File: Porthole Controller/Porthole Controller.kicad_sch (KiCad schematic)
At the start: 19 parts, among them J1 Conn_02x03_Counter_Clockwise, J2 Conn_01x03, J3 Screw_Terminal_01x03, J4 Screw_Terminal_01x03, J5 Screw_Terminal_01x03, J6 Screw_Terminal_01x03, J7 Screw_Terminal_01x02, SW1 SW_Push, U1 113991054, U2 SN74AHCT125DR

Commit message: Completed schematic
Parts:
- removed J2: Conn_01x03, symbol Connector_Generic:Conn_01x03
- removed SW1: SW_Push, symbol Switch:SW_Push
- added J2: Conn_02x04_Top_Bottom, symbol Connector_Generic:Conn_02x04_Top_Bottom
- added J8: Conn_01x04, symbol Connector_Generic:Conn_01x04
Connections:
- net L/R is gone; now on net GND: J1.1 (Pin_1)
- net 3.3V: now also J2.1 (Pin_1), J2.2 (Pin_2), J2.3 (Pin_3), J2.4 (Pin_4)
- net GND: now also J2.5 (Pin_5), J2.6 (Pin_6), J2.7 (Pin_7), J2.8 (Pin_8)
- net SCK: now also U1.10 (D9)
- net SD: now also U1.11 (D10)
- net WS: now also U1.9 (D8)
- net D0: now reaches U1.1 (D0)
- net D0: now also J8.1 (Pin_1)
- net D1: now reaches U1.2 (D1)
- net D1: now also J8.2 (Pin_2)
- net D2: now reaches U1.3 (D2)
- net D2: now also U2.2 (1A)
- net D3: now reaches U1.4 (D3)
- net D3: now also U2.5 (2A)
- net D4: now reaches U1.5 (D4)
- net D4: now also J8.3 (Pin_3)
- net D5: now reaches U1.6 (D5)
- net D5: now also J8.4 (Pin_4)
- net D6: now reaches U1.7 (TX_D6)
- net D6: now also U2.9 (3A)
- net D7: now reaches U1.8 (RX_D7)
- net D7: now also U2.12 (4A)
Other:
- moved on the sheet: J1, U1

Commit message: Prototype board designed
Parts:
- C1: value C -> 100nF; footprint (none) -> Capacitor_THT:C_Disc_D3.0mm_W1.6mm_P2.50mm
- C2, C3, C4, C5: value C_Polarized -> 1000uF; footprint (none) -> Capacitor_THT:CP_Radial_D6.3mm_P2.50mm
- J1: renamed from J3; value Screw_Terminal_01x03 -> STRIP1; footprint (none) -> TerminalBlock:TerminalBlock_bornier-3_P5.08mm
- J2: renamed from J4; value Screw_Terminal_01x03 -> STRIP2; footprint (none) -> TerminalBlock:TerminalBlock_bornier-3_P5.08mm
- J3: renamed from J5; value Screw_Terminal_01x03 -> STRIP3; footprint (none) -> TerminalBlock:TerminalBlock_bornier-3_P5.08mm
- J4: renamed from J6; value Screw_Terminal_01x03 -> STRIP4; footprint (none) -> TerminalBlock:TerminalBlock_bornier-3_P5.08mm
- J5: renamed from J1; value Conn_02x03_Counter_Clockwise -> INMP441; footprint (none) -> Connector_PinSocket_2.54mm:PinSocket_2x03_P2.54mm_Vertical; symbol Connector_Generic:Conn_02x03_Counter_Clockwise -> Connector_Generic:Conn_02x03_Odd_Even
- J6: renamed from J2; footprint (none) -> Connector_PinSocket_2.54mm:PinSocket_2x04_P2.54mm_Vertical; symbol Connector_Generic:Conn_02x04_Top_Bottom -> Connector_Generic:Conn_02x04_Odd_Even
- J7: value Screw_Terminal_01x02 -> - +; footprint (none) -> TerminalBlock:TerminalBlock_bornier-2_P5.08mm
- J8: footprint (none) -> Connector_PinSocket_2.54mm:PinSocket_1x04_P2.54mm_Vertical
- R1, R2, R3, R4: value R -> 100; footprint (none) -> Resistor_THT:R_Axial_DIN0204_L3.6mm_D1.6mm_P5.08mm_Horizontal
- U1: footprint 113991054:MODULE_113991054 -> symbols:xiaoesp32_c3_MM
- U2: footprint SN74AHCT125DR:SOIC127P600X175-14N -> symbols:N14_TEX
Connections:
- net 3.3V: now also J5.4 (Pin_4), J6.5 (Pin_5), J6.7 (Pin_7); no longer J5.5 (Pin_5), J6.2 (Pin_2), J6.4 (Pin_4)
- net GND: now also J5.2 (Pin_2), J6.2 (Pin_2), J6.4 (Pin_4); no longer J5.6 (Pin_6), J6.5 (Pin_5), J6.7 (Pin_7)
- net SCK: now also J5.5 (Pin_5); no longer J5.3 (Pin_3)
- net SD: now also J5.6 (Pin_6); no longer J5.4 (Pin_4)
- net WS: now also J5.3 (Pin_3); no longer J5.2 (Pin_2)
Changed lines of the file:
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@@
 	)
 	(symbol
-		(lib_id "Connector_Generic:Conn_02x04_Top_Bottom")
+		(lib_id "Connector_Generic:Conn_02x04_Odd_Even")
 		(at 85.09 142.24 0)
 		(unit 1)
@@
 		(dnp no)
 		(fields_autoplaced yes)
-		(property "Reference" "J2"
+		(property "Reference" "J6"
 			(at 86.36 133.35 0)
 			(effects
@@
 			)
 		)
-		(property "Footprint" ""
+		(property "Footprint" "Connector_PinSocket_2.54mm:PinSocket_2x04_P2.54mm_Vertical"
 			(at 85.09 142.24 0)
 			(effects
@@
 			)
 		)
-		(property "Description" "Generic connector, double row, 02x04, top/bottom pin numbering scheme (row 1: 1...pins_per_row, row2: pins_per_row+1 ... num_pins), script generated (kicad-library-utils/schlib/autogen/connector/)"
+		(property "Description" "Generic connector, double row, 02x04, odd/even pin numbering scheme (row 1 odd numbers, row 2 even numbers), script generated (kicad-library-utils/schlib/autogen/connector/)"
 			(at 85.09 142.24 0)
 			(effects
@@
 			(project "Porthole Controller"
 				(path "/13f1af3d-398f-4c37-b3cd-b8dafcc64830"
-					(reference "J2")
+					(reference "J6")
 					(unit 1)
 				)
@@
 			)
 		)
-		(property "Footprint" ""
+		(property "Footprint" "Connector_PinSocket_2.54mm:PinSocket_1x04_P2.54mm_Vertical"
 			(at 58.42 142.24 0)
 			(effects
@@
 			)
 		)
-		(property "Value" "C_Polarized"
+		(property "Value" "1000uF"
 			(at 207.01 141.3509 0)
 			(effects
@@
 			)
 		)
-		(property "Footprint" ""
+		(property "Footprint" "Capacitor_THT:CP_Radial_D6.3mm_P2.50mm"
 			(at 204.1652 144.78 0)
 			(effects
@@
 		(on_board yes)
 		(dnp no)
-		(fields_autoplaced yes)
 		(property "Reference" "R1"
-			(at 220.9801 40.64 0)
-			(effects
-				(font
-					(size 1.27 1.27)
-				)
-				(justify left)
-			)
-		)
-		(property "Value" "R"
-			(at 218.4401 40.64 0)
-			(effects
-				(font
-					(size 1.27 1.27)
-				)
-				(justify left)
-			)
-		)
-		(property "Footprint" ""
+			(at 219.964 35.814 90)
+			(effects
+				(font
+					(size 1.27 1.27)
+				)
+			)
+		)
+		(property "Value" "100"
+			(at 219.71 38.1 90)
+			(effects
+				(font
+					(size 1.27 1.27)
+				)
+			)
+		)
+		(property "Footprint" "Resistor_THT:R_Axial_DIN0204_L3.6mm_D1.6mm_P5.08mm_Horizontal"
 			(at 219.71 36.322 90)
 			(effects
@@
 			)
 		)
-		(property "Value" "C_Polarized"
+		(property "Value" "1000uF"
 			(at 207.01 115.9509 0)
 			(effects
@@
 			)
 		)
-		(property "Footprint" ""
+		(property "Footprint" "Capacitor_THT:CP_Radial_D6.3mm_P2.50mm"
 			(at 204.1652 119.38 0)
 			(effects
@@
 			)
 		)
-		(property "Value" "C"
+		(property "Value" "100nF"
 			(at 210.82 55.8799 0)
 			(effects
@@
 			)
 		)
-		(property "Footprint" ""
+		(property "Footprint" "Capacitor_THT:C_Disc_D3.0mm_W1.6mm_P2.50mm"
 			(at 207.9752 58.42 0)
 			(effects
@@
 			)
 		)
-		(property "Value" "Screw_Terminal_01x02"
+		(property "Value" "-   +"
 			(at 110.49 36.8299 0)
 			(effects
@@
 			)
 		)
-		(property "Footprint" ""
+		(property "Footprint" "TerminalBlock:TerminalBlock_bornier-2_P5.08mm"
 			(at 107.95 34.29 0)
 			(effects
@@
 		(on_board yes)
 		(dnp no)
-		(fields_autoplaced yes)
 		(property "Reference" "R4"
-			(at 220.9801 63.5 0)
-			(effects
-				(font
-					(size 1.27 1.27)
-				)
-				(justify left)
-			)
-		)
-		(property "Value" "R"
-			(at 218.4401 63.5 0)
-			(effects
-				(font
-					(size 1.27 1.27)
-				)
-				(justify left)
-			)
-		)
-		(property "Footprint" ""
+			(at 219.71 58.674 90)
+			(effects
+				(font
+					(size 1.27 1.27)
+				)
+			)
+		)
+		(property "Value" "100"
+			(at 219.71 60.96 90)
+			(effects
+				(font
+					(size 1.27 1.27)
+				)
+			)
+		)
+		(property "Footprint" "Resistor_THT:R_Axial_DIN0204_L3.6mm_D1.6mm_P5.08mm_Horizontal"
 			(at 219.71 59.182 90)
 			(effects
@@
 	)
 	(symbol
-		(lib_id "Connector_Generic:Conn_02x03_Counter_Clockwise")
+		(lib_id "Connector_Generic:Conn_02x03_Odd_Even")
 		(at 135.89 96.52 0)
 		(unit 1)
@@
 		(dnp no)
 		(fields_autoplaced yes)
-		(property "Reference" "J1"
+		(property "Reference" "J5"
 			(at 137.16 87.63 0)
 			(effects
@@
 			)
 		)
-		(property "Value" "Conn_02x03_Counter_Clockwise"
+		(property "Value" "INMP441"
 			(at 137.16 90.17 0)
 			(effects
@@
 			)
 		)
-		(property "Footprint" ""
+		(property "Footprint" "Connector_PinSocket_2.54mm:PinSocket_2x03_P2.54mm_Vertical"
 			(at 135.89 96.52 0)
 			(effects
@@
 			)
 		)
-		(property "Description" "Generic connector, double row, 02x03, counter clockwise pin numbering scheme (similar to DIP package numbering), script generated (kicad-library-utils/schlib/autogen/connector/)"
+		(property "Description" "Generic connector, double row, 02x03, odd/even pin numbering scheme (row 1 odd numbers, row 2 even numbers), script generated (kicad-library-utils/schlib/autogen/connector/)"
 			(at 135.89 96.52 0)
 			(effects
@@
 			(project "Porthole Controller"
 				(path "/13f1af3d-398f-4c37-b3cd-b8dafcc64830"
-					(reference "J1")
+					(reference "J5")
 					(unit 1)
 				)
@@
 			)
 		)
-		(property "Value" "C_Polarized"
+		(property "Value" "1000uF"
 			(at 207.01 101.9809 0)
 			(effects
@@
 			)
 		)
-		(property "Footprint" ""
+		(property "Footprint" "Capacitor_THT:CP_Radial_D6.3mm_P2.50mm"
 			(at 204.1652 105.41 0)
 			(effects
@@
 		(dnp no)
 		(fields_autoplaced yes)
-		(property "Reference" "J3"
+		(property "Reference" "J1"
 			(at 223.52 100.3299 0)
 			(effects
@@
 			)
 		)
-		(property "Value" "Screw_Terminal_01x03"
+		(property "Value" "STRIP1"
 			(at 223.52 102.8699 0)
 			(effects
@@
 			)
 		)
-		(property "Footprint" ""
+		(property "Footprint" "TerminalBlock:TerminalBlock_bornier-3_P5.08mm"
 			(at 220.98 101.6 0)
 			(effects
@@
 			(project "Porthole Controller"
 				(path "/13f1af3d-398f-4c37-b3cd-b8dafcc64830"
-					(reference "J3")
+					(reference "J1")
 					(unit 1)
 				)
@@
 		(on_board yes)
 		(dnp no)
-		(fields_autoplaced yes)
 		(property "Reference" "R2"
-			(at 220.9801 48.26 0)
-			(effects
-				(font
-					(size 1.27 1.27)
-				)
-				(justify left)
-			)
-		)
-		(property "Value" "R"
-			(at 218.4401 48.26 0)
-			(effects
-				(font
-					(size 1.27 1.27)
-				)
-				(justify left)
-			)
-		)
-		(property "Footprint" ""
+			(at 218.186 43.434 90)
+			(effects
+				(font
+					(size 1.27 1.27)
+				)
+				(justify left)
+			)
+		)
+		(property "Value" "100"
+			(at 217.678 45.72 90)
+			(effects
+				(font
+					(size 1.27 1.27)
+				)
+				(justify left)
+			)
+		)
+		(property "Footprint" "Resistor_THT:R_Axial_DIN0204_L3.6mm_D1.6mm_P5.08mm_Horizontal"
 			(at 219.71 43.942 90)
 			(effects
@@
 		(dnp no)
 		(fields_autoplaced yes)
-		(property "Reference" "J5"
+		(property "Reference" "J3"
 			(at 223.52 125.7299 0)
 			(effects
@@
 			)
 		)
-		(property "Value" "Screw_Terminal_01x03"
+		(property "Value" "STRIP3"
 			(at 223.52 128.2699 0)
 			(effects
@@
 			)
 		)
-		(property "Footprint" ""
+		(property "Footprint" "TerminalBlock:TerminalBlock_bornier-3_P5.08mm"
 			(at 220.98 127 0)
 			(effects
@@
 			(project "Porthole Controller"
 				(path "/13f1af3d-398f-4c37-b3cd-b8dafcc64830"
-					(reference "J5")
+					(reference "J3")
 					(unit 1)
 				)
@@
 			)
 		)
-		(property "Value" "C_Polarized"
+		(property "Value" "1000uF"
 			(at 207.01 127.3809 0)
 			(effects
@@
 			)
 		)
-		(property "Footprint" ""
+		(property "Footprint" "Capacitor_THT:CP_Radial_D6.3mm_P2.50mm"
 			(at 204.1652 130.81 0)
 			(effects
@@
 		(on_board yes)
 		(dnp no)
-		(fields_autoplaced yes)
 		(property "Reference" "R3"
-			(at 220.9801 55.88 0)
-			(effects
-				(font
-					(size 1.27 1.27)
-				)
-				(justify left)
-			)
-		)
-		(property "Value" "R"
-			(at 218.4401 55.88 0)
-			(effects
-				(font
-					(size 1.27 1.27)
-				)
-				(justify left)
-			)
-		)
-		(property "Footprint" ""
+			(at 219.964 51.054 90)
+			(effects
+				(font
+					(size 1.27 1.27)
+				)
+			)
+		)
+		(property "Value" "100"
+			(at 219.71 53.34 90)
+			(effects
+				(font
+					(size 1.27 1.27)
+				)
+			)
+		)
+		(property "Footprint" "Resistor_THT:R_Axial_DIN0204_L3.6mm_D1.6mm_P5.08mm_Horizontal"
 			(at 219.71 51.562 90)
 			(effects
@@
 			)
 		)
-		(property "Footprint" "113991054:MODULE_113991054"
+		(property "Footprint" "symbols:xiaoesp32_c3_MM"
 			(at 83.82 99.06 0)
 			(effects
@@
 			)
 		)
-		(property "Footprint" "SN74AHCT125DR:SOIC127P600X175-14N"
+		(property "Footprint" "symbols:N14_TEX"
 			(at 184.15 48.26 0)
 			(effects
@@
 		(dnp no)
 		(fields_autoplaced yes)
-		(property "Reference" "J4"
+		(property "Reference" "J2"
 			(at 223.52 114.2999 0)
 			(effects
@@
 			)
 		)
-		(property "Value" "Screw_Terminal_01x03"
+		(property "Value" "STRIP2"
 			(at 223.52 116.8399 0)
 			(effects
@@
 			)
 		)
-		(property "Footprint" ""
+		(property "Footprint" "TerminalBlock:TerminalBlock_bornier-3_P5.08mm"
 			(at 220.98 115.57 0)
 			(effects
@@
 			(project "Porthole Controller"
 				(path "/13f1af3d-398f-4c37-b3cd-b8dafcc64830"
-					(reference "J4")
+					(reference "J2")
 					(unit 1)
 				)
@@
 		(dnp no)
 		(fields_autoplaced yes)
-		(property "Reference" "J6"
+		(property "Reference" "J4"
 			(at 223.52 139.6999 0)
 			(effects
@@
 			)
 		)
-		(property "Value" "Screw_Terminal_01x03"
+		(property "Value" "STRIP4"
 			(at 223.52 142.2399 0)
 			(effects
@@
 			)
 		)
-		(property "Footprint" ""
+		(property "Footprint" "TerminalBlock:TerminalBlock_bornier-3_P5.08mm"
 			(at 220.98 140.97 0)
 			(effects
@@
 			(project "Porthole Controller"
 				(path "/13f1af3d-398f-4c37-b3cd-b8dafcc64830"
-					(reference "J6")
-					(unit 1)
-				)
+					(reference "J4")
+					(unit 1)
+				)

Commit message: Updated footprints
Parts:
- C2, C3, C4, C5: footprint Capacitor_THT:CP_Radial_D6.3mm_P2.50mm -> Capacitor_THT:CP_Radial_D8.0mm_P3.80mm
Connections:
- net 3.3V: now also J5.3 (Pin_3); no longer J5.4 (Pin_4)
- net SCK: now also J5.6 (Pin_6), U1.9 (D8); no longer J5.5 (Pin_5), U1.10 (D9)
- net SD: now also J5.5 (Pin_5); no longer J5.6 (Pin_6)
- net WS: now also J5.4 (Pin_4), U1.10 (D9); no longer J5.3 (Pin_3), U1.9 (D8)

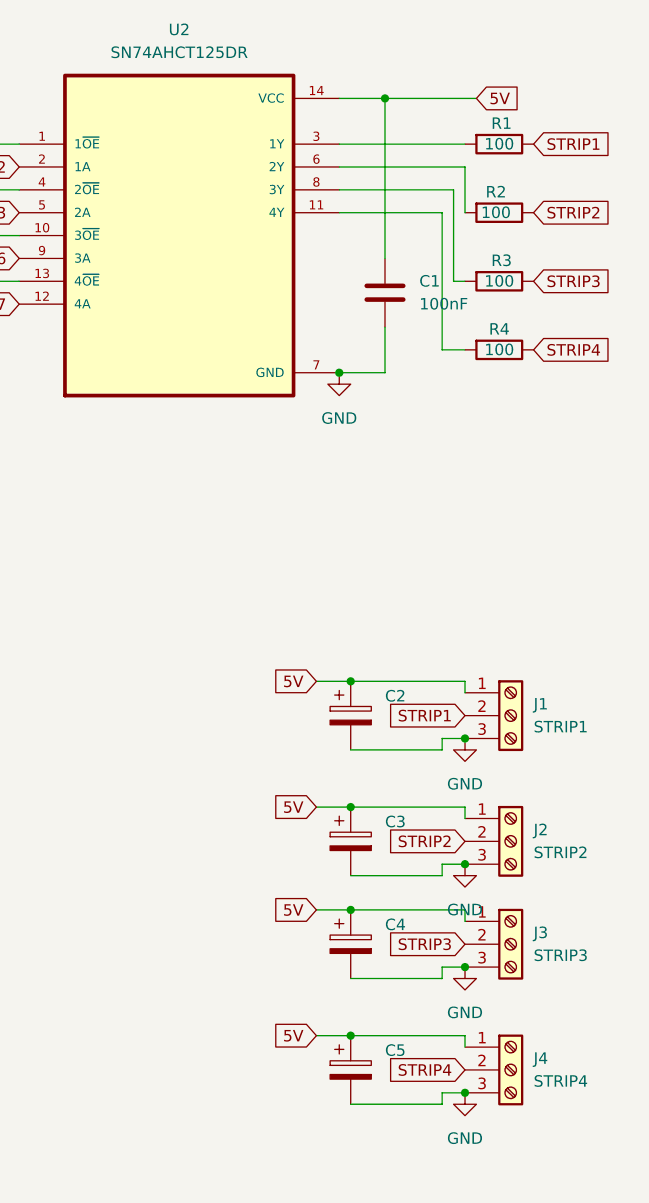
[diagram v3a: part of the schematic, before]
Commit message: bolden text, fix capacitor labels, reviewed DRC warnings
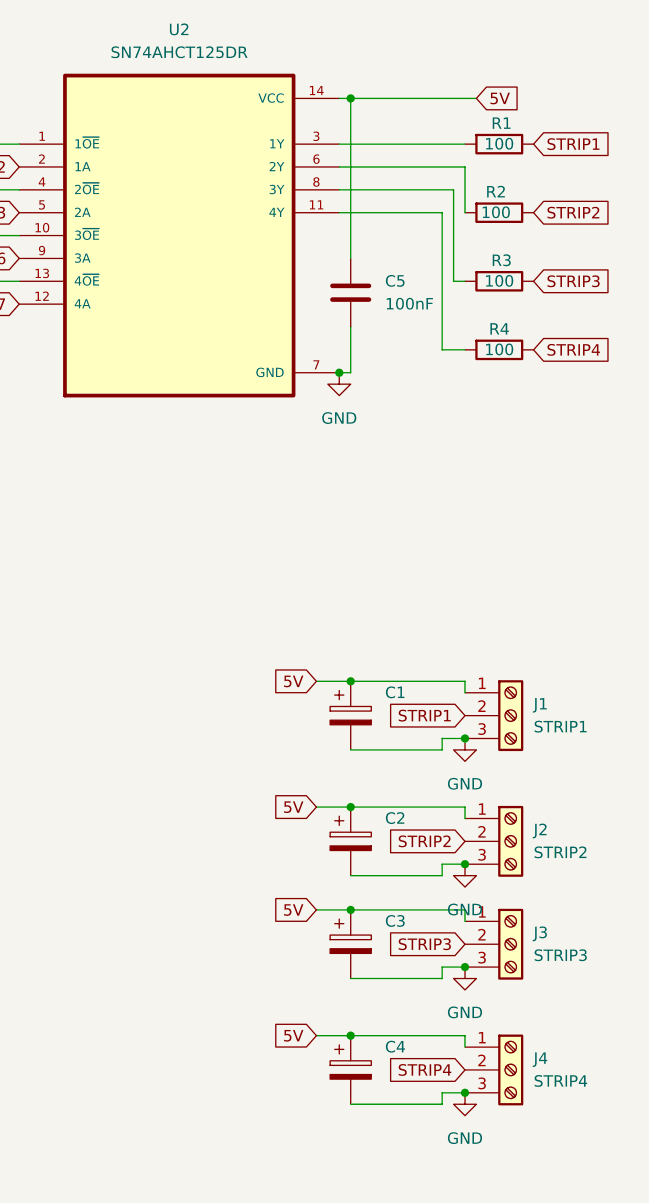
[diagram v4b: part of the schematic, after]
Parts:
- renumbered C2 to C1, C3 to C2, C4 to C3, C5 to C4, C1 to C5
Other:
- moved on the sheet: C5
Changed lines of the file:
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@@
 	)
 	(junction
-		(at 201.93 63.5)
+		(at 203.2 33.02)
 		(diameter 0)
 		(color 0 0 0 0)
 	)
 	(junction
-		(at 215.9 143.51)
+		(at 201.93 63.5)
 		(diameter 0)
 		(color 0 0 0 0)
 	)
 	(junction
-		(at 215.9 129.54)
+		(at 215.9 143.51)
 		(diameter 0)
 		(color 0 0 0 0)
 	)
 	(junction
-		(at 207.01 33.02)
+		(at 215.9 129.54)
 		(diameter 0)
 		(color 0 0 0 0)
@@
 	(wire
 		(pts
+			(xy 203.2 33.02) (xy 201.93 33.02)
+		)
+		(stroke
+			(width 0)
+			(type default)
+		)
+	)
+	(wire
+		(pts
 			(xy 215.9 111.76) (xy 215.9 113.03)
 		)
@@
 	(wire
 		(pts
-			(xy 207.01 63.5) (xy 201.93 63.5)
+			(xy 203.2 63.5) (xy 201.93 63.5)
 		)
 		(stroke
@@
 	(wire
 		(pts
-			(xy 207.01 58.42) (xy 207.01 63.5)
+			(xy 203.2 58.42) (xy 203.2 63.5)
 		)
 		(stroke
@@
 	(wire
 		(pts
-			(xy 207.01 50.8) (xy 207.01 33.02)
+			(xy 203.2 50.8) (xy 203.2 33.02)
 		)
 		(stroke
@@
 	(wire
 		(pts
-			(xy 203.2 123.19) (xy 215.9 123.19)
-		)
-		(stroke
-			(width 0)
-			(type default)
-		)
-	)
-	(wire
-		(pts
-			(xy 207.01 33.02) (xy 201.93 33.02)
+			(xy 203.2 33.02) (xy 217.17 33.02)
 		)
 		(stroke
@@
 	(wire
 		(pts
-			(xy 217.17 33.02) (xy 207.01 33.02)
+			(xy 203.2 123.19) (xy 215.9 123.19)
 		)
 		(stroke
@@
 		(on_board yes)
 		(dnp no)
-		(fields_autoplaced yes)
-		(property "Reference" "C5"
-			(at 207.01 138.8109 0)
+		(property "Reference" "C4"
+			(at 207.01 138.43 0)
 			(effects
 				(font
@@
 			(project "Porthole Controller"
 				(path "/13f1af3d-398f-4c37-b3cd-b8dafcc64830"
-					(reference "C5")
+					(reference "C4")
 					(unit 1)
 				)
@@
 		(on_board yes)
 		(dnp no)
-		(fields_autoplaced yes)
-		(property "Reference" "C3"
-			(at 207.01 113.4109 0)
+		(property "Reference" "C2"
+			(at 207.01 113.03 0)
 			(effects
 				(font
@@
 			(project "Porthole Controller"
 				(path "/13f1af3d-398f-4c37-b3cd-b8dafcc64830"
-					(reference "C3")
+					(reference "C2")
 					(unit 1)
 				)
@@
 	(symbol
 		(lib_id "Device:C")
-		(at 207.01 54.61 0)
+		(at 203.2 54.61 0)
 		(unit 1)
 		(exclude_from_sim no)
@@
 		(dnp no)
 		(fields_autoplaced yes)
-		(property "Reference" "C1"
-			(at 210.82 53.3399 0)
+		(property "Reference" "C5"
+			(at 207.01 53.3399 0)
 			(effects
 				(font
@@
 		)
 		(property "Value" "100nF"
-			(at 210.82 55.8799 0)
+			(at 207.01 55.8799 0)
 			(effects
 				(font
@@
 		)
 		(property "Footprint" "Capacitor_THT:C_Disc_D3.0mm_W1.6mm_P2.50mm"
-			(at 207.9752 58.42 0)
+			(at 204.1652 58.42 0)
 			(effects
 				(font
@@
 		)
 		(property "Datasheet" "~"
-			(at 207.01 54.61 0)
+			(at 203.2 54.61 0)
 			(effects
 				(font
@@
 		)
 		(property "Description" "Unpolarized capacitor"
-			(at 207.01 54.61 0)
+			(at 203.2 54.61 0)
 			(effects
 				(font
@@
 			(project "Porthole Controller"
 				(path "/13f1af3d-398f-4c37-b3cd-b8dafcc64830"
-					(reference "C1")
+					(reference "C5")
 					(unit 1)
 				)
@@
 		(on_board yes)
 		(dnp no)
-		(fields_autoplaced yes)
-		(property "Reference" "C2"
-			(at 207.01 99.4409 0)
+		(property "Reference" "C1"
+			(at 207.01 99.06 0)
 			(effects
 				(font
@@
 			(project "Porthole Controller"
 				(path "/13f1af3d-398f-4c37-b3cd-b8dafcc64830"
-					(reference "C2")
+					(reference "C1")
 					(unit 1)
 				)
@@
 		(on_board yes)
 		(dnp no)
-		(fields_autoplaced yes)
-		(property "Reference" "C4"
-			(at 207.01 124.8409 0)
+		(property "Reference" "C3"
+			(at 207.01 124.46 0)
 			(effects
 				(font
@@
 			(project "Porthole Controller"
 				(path "/13f1af3d-398f-4c37-b3cd-b8dafcc64830"
-					(reference "C4")
+					(reference "C3")
 					(unit 1)
 				)
